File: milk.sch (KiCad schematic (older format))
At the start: 20 parts, among them J1 USB_C_Receptacle_USB2.0, J3 RGB, J4 PB3|PB4, SW1 SW_Push, SW2 SW_Push, SW3 SW_Push_Reset, U1 ATtiny85-20SU

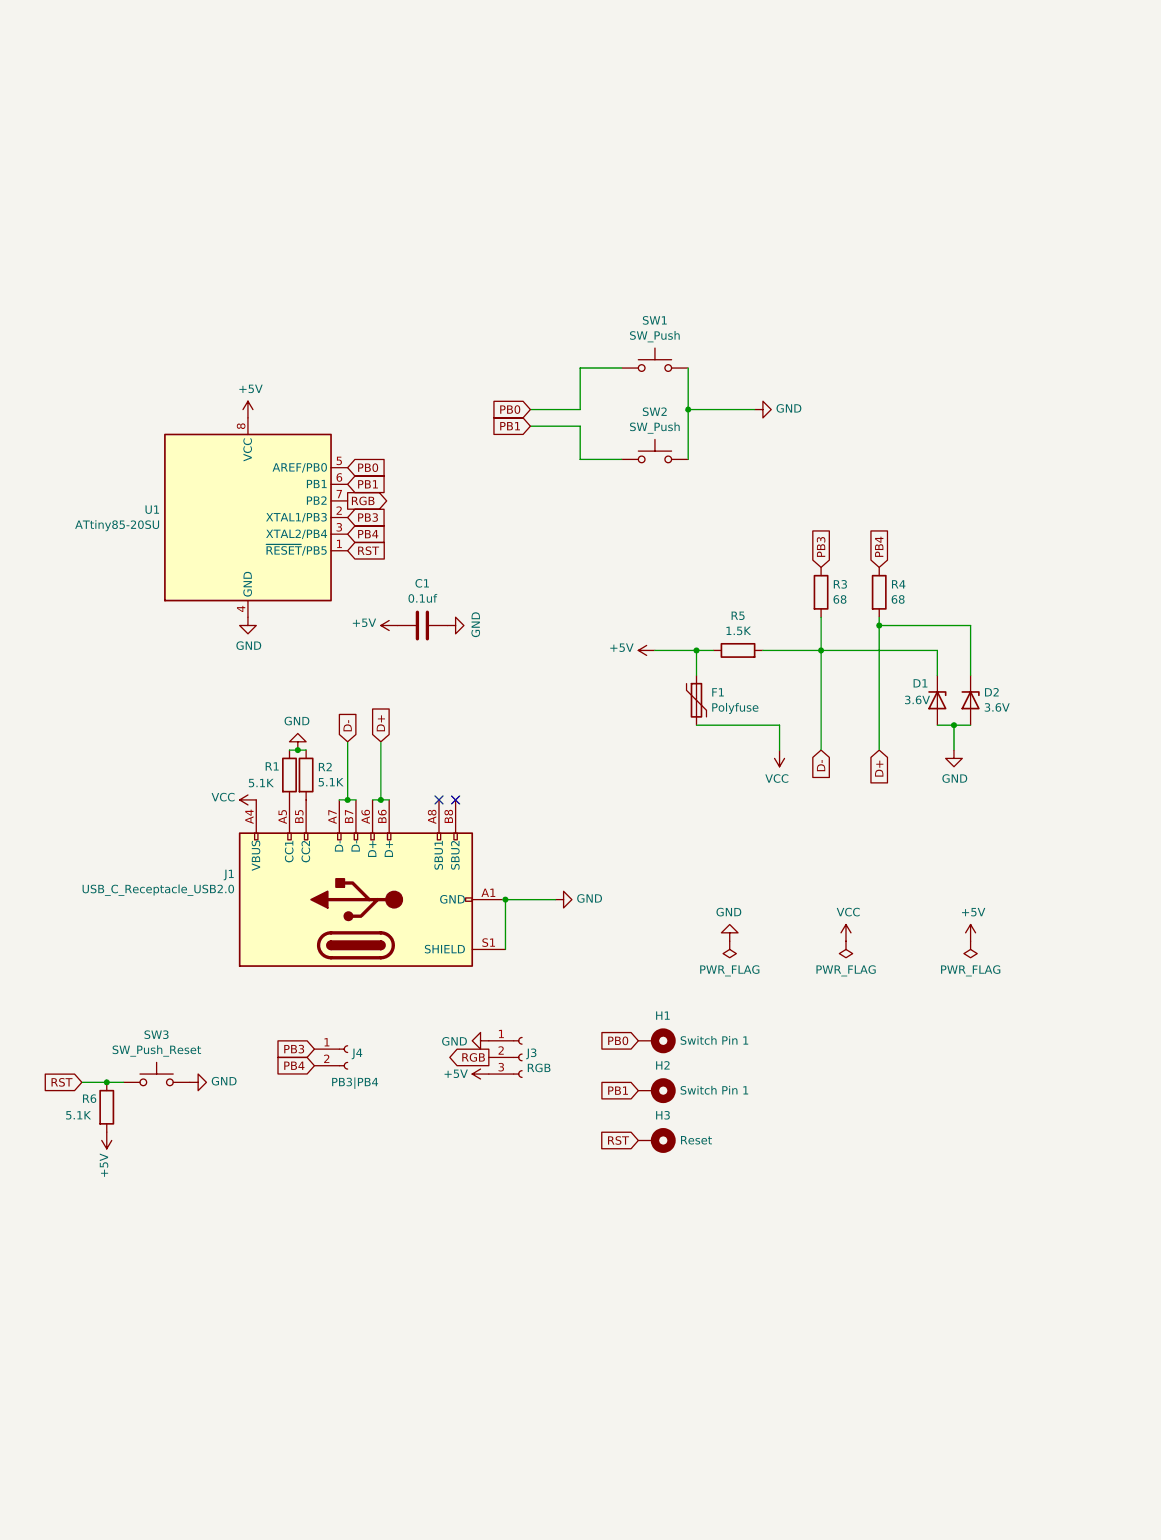
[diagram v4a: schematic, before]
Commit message: Change programming header for a DIP-8 package, compatible with ATtiny85-20PU
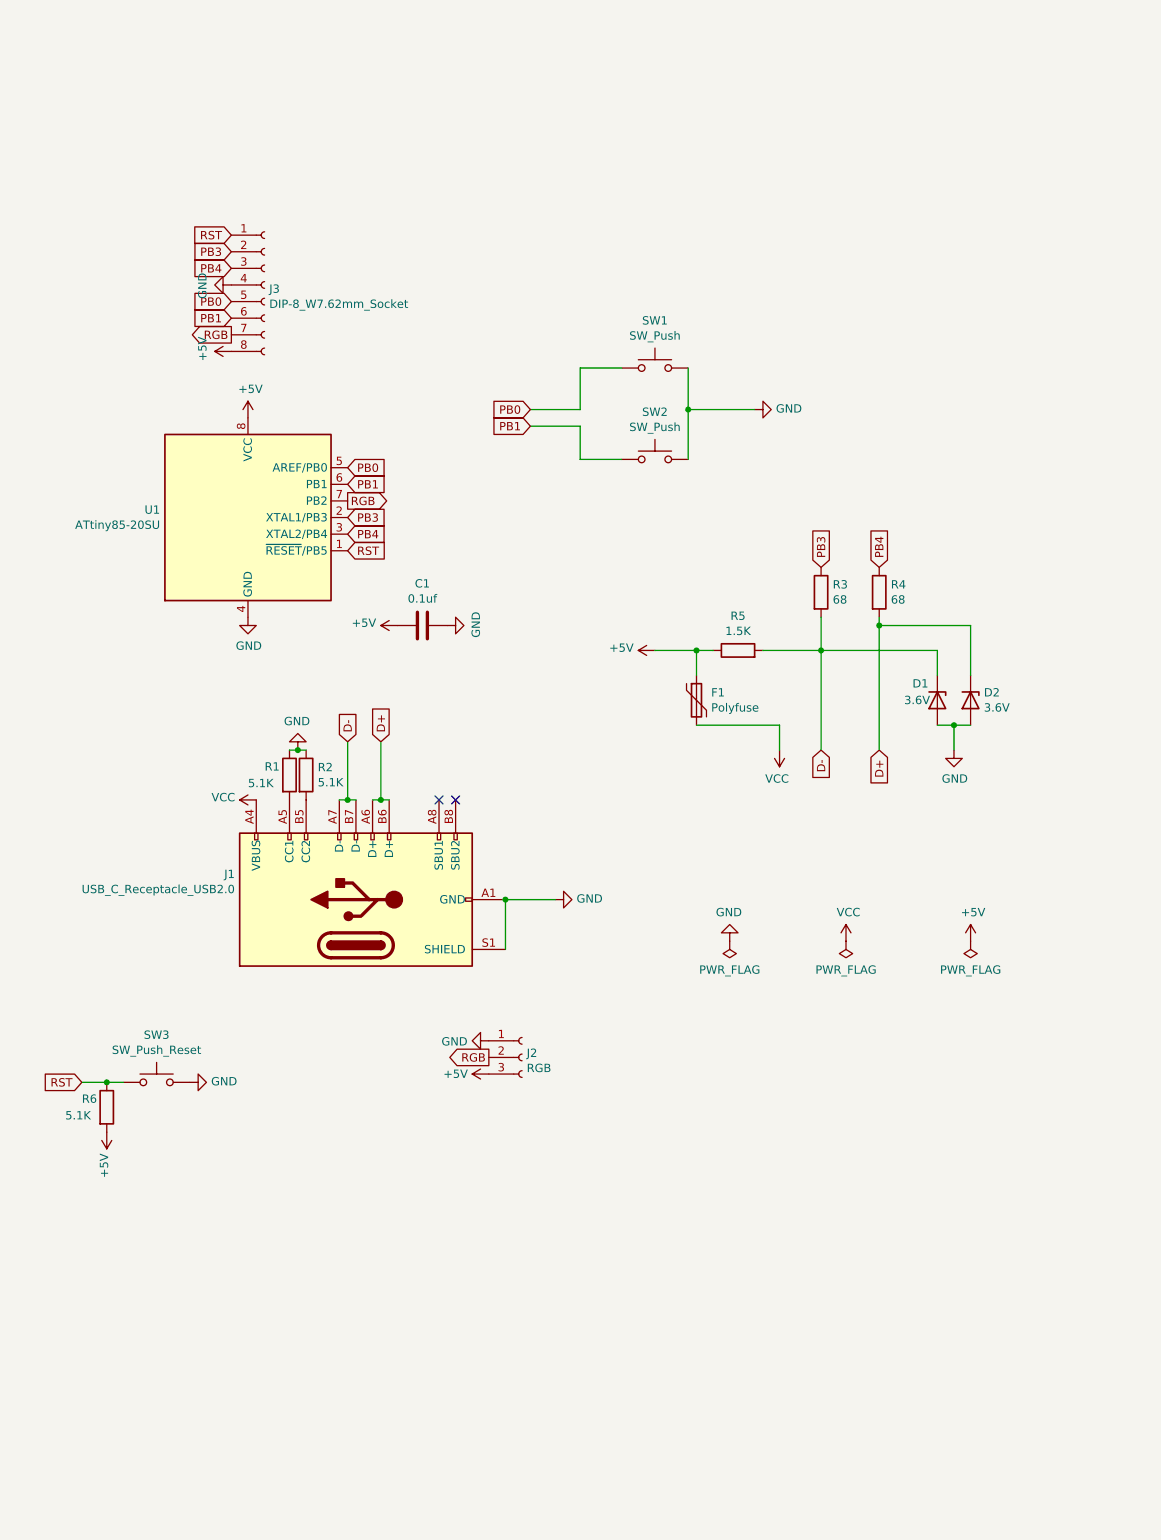
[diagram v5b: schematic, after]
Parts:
- removed H1, H2: Switch Pin 1, TestPoint:TestPoint_THTPad_D1.5mm_Drill0.7mm, symbol Mechanical:MountingHole_Pad
- removed H3: Reset, TestPoint:TestPoint_THTPad_D1.5mm_Drill0.7mm, symbol Mechanical:MountingHole_Pad
- removed J4: PB3|PB4, Connector_PinHeader_2.54mm:PinHeader_1x02_P2.54mm_Vertical, symbol Connector:Conn_01x02_Female
- added J3: DIP-8_W7.62mm_Socket, Package_DIP:DIP-8_W7.62mm_Socket, symbol Connector:Conn_01x08_Female
- renumbered J3 to J2
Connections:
- net +5V: now also J3.8 (Pin_8)
- net GND: now also J3.4 (Pin_4)
- net PB0: now also J3.5 (Pin_5)
- net PB1: now also J3.6 (Pin_6)
- net PB3: now also J3.2 (Pin_2)
- net PB4: now also J3.3 (Pin_3)
- net RGB: now also J3.7 (Pin_7)
- net RST: now also J3.1 (Pin_1)
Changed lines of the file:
@@
 $EndComp
 $Comp
-L Connector:Conn_01x03_Female J3
+L Connector:Conn_01x03_Female J2
 U 1 1 5CCEB648
 P 3700 7300
-F 0 "J3" H 3728 7326 50  0000 L CNN
+F 0 "J2" H 3728 7326 50  0000 L CNN
 F 1 "RGB" H 3728 7235 50  0000 L CNN
 F 2 "Connector_PinHeader_2.54mm:PinHeader_1x03_P2.54mm_Vertical" H 3700 7300 50  0001 C CNN
@@
 	1    3500 7400
 	0    -1   -1   0
-$EndComp
-$Comp
-L Connector:Conn_01x02_Female J4
-U 1 1 612A3118
-P 2650 7250
-F 0 "J4" H 2678 7226 50  0000 L CNN
-F 1 "PB3|PB4" H 2550 7050 50  0000 L CNN
-F 2 "Connector_PinHeader_2.54mm:PinHeader_1x02_P2.54mm_Vertical" H 2650 7250 50  0001 C CNN
-F 3 "~" H 2650 7250 50  0001 C CNN
-	1    2650 7250
-	1    0    0    -1
-$EndComp
-$Comp
-L Mechanical:MountingHole_Pad H1
-U 1 1 612D4988
-P 4500 7200
-F 0 "H1" V 4350 7200 50  0000 L CNN
-F 1 "Switch Pin 1" V 4500 7350 50  0000 L CNN
-F 2 "TestPoint:TestPoint_THTPad_D1.5mm_Drill0.7mm" H 4500 7200 50  0001 C CNN
-F 3 "~" H 4500 7200 50  0001 C CNN
-	1    4500 7200
-	0    1    1    0
 $EndComp
 $Comp
@@
 Text GLabel 2650 3850 2    50   Input ~ 0
 PB1
-$Comp
-L Mechanical:MountingHole_Pad H2
-U 1 1 612DFE3A
-P 4500 7500
-F 0 "H2" V 4350 7500 50  0000 L CNN
-F 1 "Switch Pin 1" V 4500 7650 50  0000 L CNN
-F 2 "TestPoint:TestPoint_THTPad_D1.5mm_Drill0.7mm" H 4500 7500 50  0001 C CNN
-F 3 "~" H 4500 7500 50  0001 C CNN
-	1    4500 7500
-	0    1    1    0
-$EndComp
-Text GLabel 4400 7200 0    50   Input ~ 0
-PB0
-Text GLabel 4400 7500 0    50   Input ~ 0
-PB1
 Text GLabel 5500 4350 1    50   Input ~ 0
 PB3
@@
 	1    0    0    -1
 $EndComp
-Text GLabel 2450 7350 0    50   Input ~ 0
-PB4
-Text GLabel 2450 7250 0    50   Input ~ 0
-PB3
 $Comp
 L power:GND #PWR0107
@@
 $EndComp
 Text GLabel 1050 7450 0    50   Input ~ 0
-RST
-$Comp
-L Mechanical:MountingHole_Pad H3
-U 1 1 612C7A56
-P 4500 7800
-F 0 "H3" V 4350 7800 50  0000 L CNN
-F 1 "Reset" V 4500 7950 50  0000 L CNN
-F 2 "TestPoint:TestPoint_THTPad_D1.5mm_Drill0.7mm" H 4500 7800 50  0001 C CNN
-F 3 "~" H 4500 7800 50  0001 C CNN
-	1    4500 7800
-	0    1    1    0
-$EndComp
-Text GLabel 4400 7800 0    50   Input ~ 0
 RST
 Wire Wire Line
@@
 	-1   0    0    1
 $EndComp
+$Comp
+L Connector:Conn_01x08_Female J3
+U 1 1 612C5061
+P 2150 2650
+F 0 "J3" H 2178 2626 50  0000 L CNN
+F 1 "DIP-8_W7.62mm_Socket" H 2178 2535 50  0000 L CNN
+F 2 "Package_DIP:DIP-8_W7.62mm_Socket" H 2150 2650 50  0001 C CNN
+F 3 "~" H 2150 2650 50  0001 C CNN
+	1    2150 2650
+	1    0    0    -1
+$EndComp
+Text GLabel 1950 2750 0    50   Input ~ 0
+PB0
+Text GLabel 1950 2850 0    50   Input ~ 0
+PB1
+Text GLabel 1950 2950 0    50   Output ~ 0
+RGB
+$Comp
+L power:+5V #PWR?
+U 1 1 612C72C8
+P 1950 3050
+F 0 "#PWR?" H 1950 2900 50  0001 C CNN
+F 1 "+5V" H 1965 3223 50  0000 C CNN
+F 2 "" H 1950 3050 50  0001 C CNN
+F 3 "" H 1950 3050 50  0001 C CNN
+	1    1950 3050
+	0    -1   -1   0
+$EndComp
+Text GLabel 1950 2350 0    50   Input ~ 0
+RST
+Text GLabel 1950 2450 0    50   Input ~ 0
+PB3
+Text GLabel 1950 2550 0    50   Input ~ 0
+PB4
+$Comp
+L power:GND #PWR?
+U 1 1 612C7D5C
+P 1950 2650
+F 0 "#PWR?" H 1950 2400 50  0001 C CNN
+F 1 "GND" H 1955 2477 50  0000 C CNN
+F 2 "" H 1950 2650 50  0001 C CNN
+F 3 "" H 1950 2650 50  0001 C CNN
+	1    1950 2650
+	0    1    1    0
+$EndComp
 $EndSCHEMATC

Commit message: Redo routing, add unsolderable RGB leds
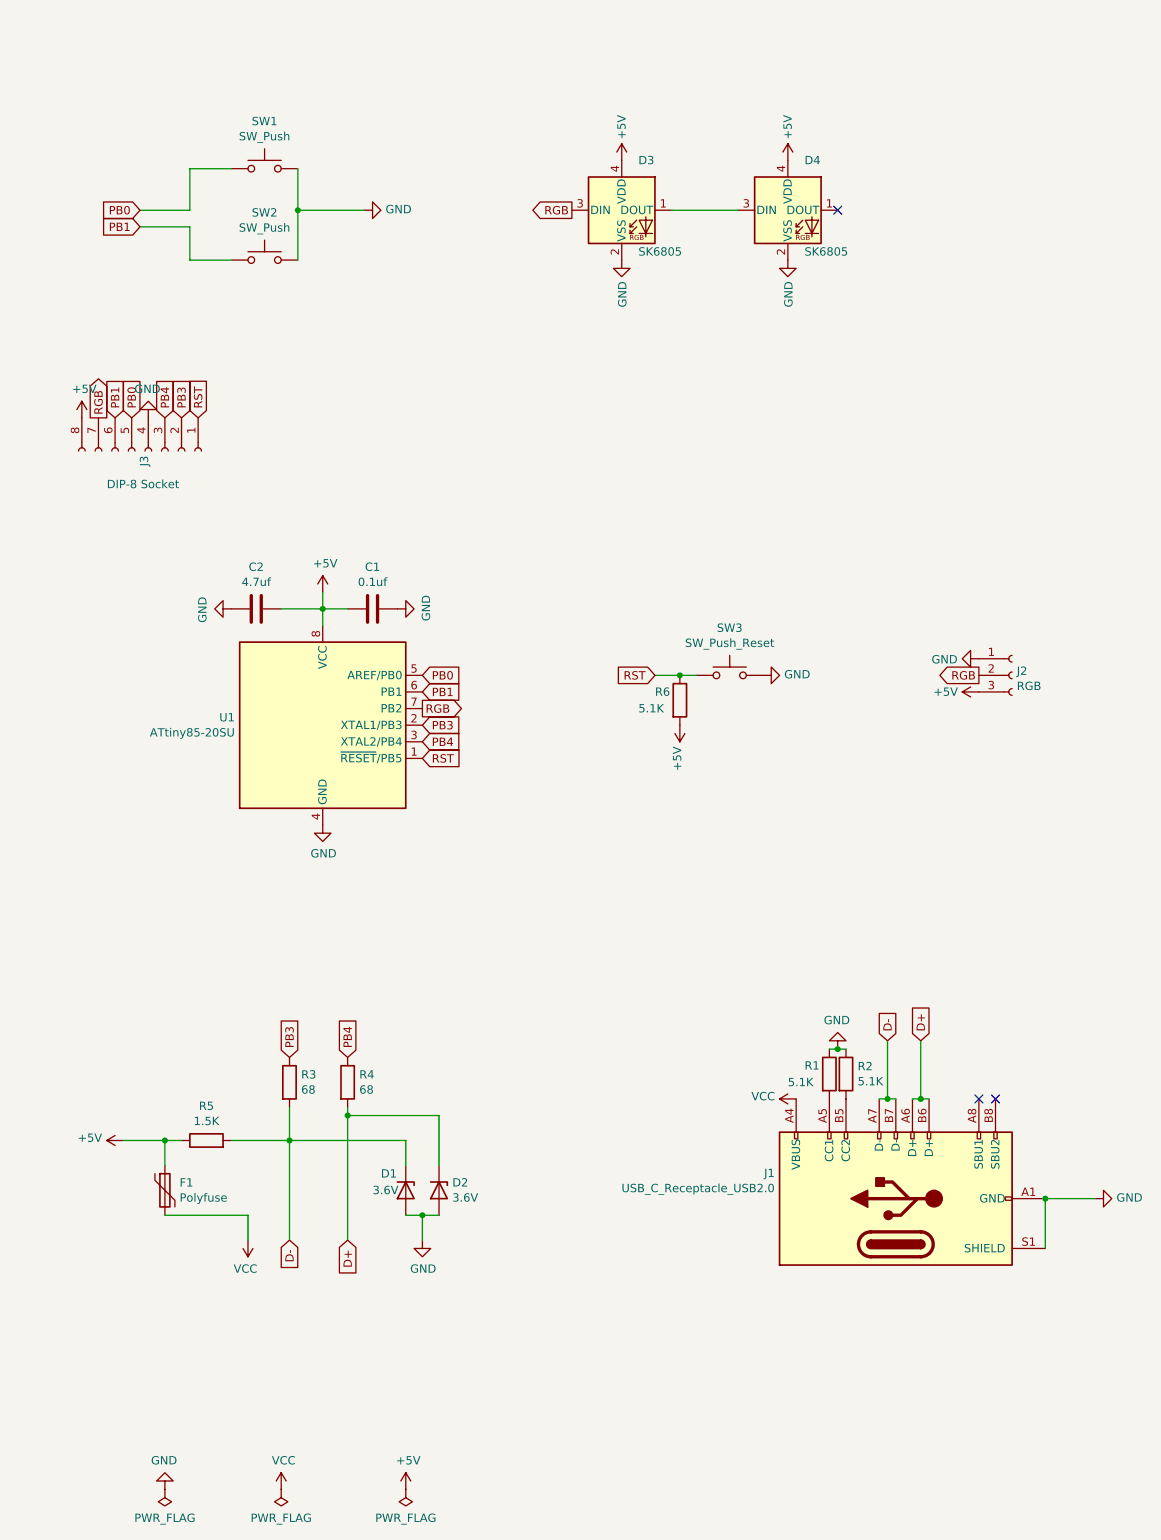
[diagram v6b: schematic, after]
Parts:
- added C2: 4.7uf, Capacitor_SMD:C_0805_2012Metric_Pad1.18x1.45mm_HandSolder, symbol Device:C
- added D3, D4: SK6805, LED_SMD:LED_SK6812_EC15_1.5x1.5mm, symbol LED:SK6805
- J3: value DIP-8_W7.62mm_Socket -> DIP-8 Socket
- SW1, SW2: footprint Button_Switch_Keyboard:SW_Cherry_MX_1.00u_PCB -> footprints:SW_Cherry_MX_1.00u_PCB-2mm
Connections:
- net +5V: now also C2.2, D3.4 (VDD), D4.4 (VDD)
- net GND: now also C2.1, D3.2 (VSS), D4.2 (VSS)
- net RGB: now also D3.3 (DIN)
- new net: D3.1 (DOUT), D4.3 (DIN)
- no-connect marks 2 -> 3
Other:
- moved on the sheet: C1, D1, D2, F1, J1, J2, J3, R1, R2, R3, R4, R5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
